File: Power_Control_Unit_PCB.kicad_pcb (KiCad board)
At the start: 2 copper layers, 98.3 x 93.2 mm, 25 parts, among them J1 Molex_Conn_01x04, J2 WR-BHD_Conn_02x08_Odd_Even, J3 WR-BHD_Conn_02x04_Odd_Even, J4 WR-BHD_Conn_02x03_Odd_Even, J5 WR-BHD_Conn_02x17_Odd_Even, U1 TSR_1-2433, U2 TSR_1-2450, U3 TSR3-24120N

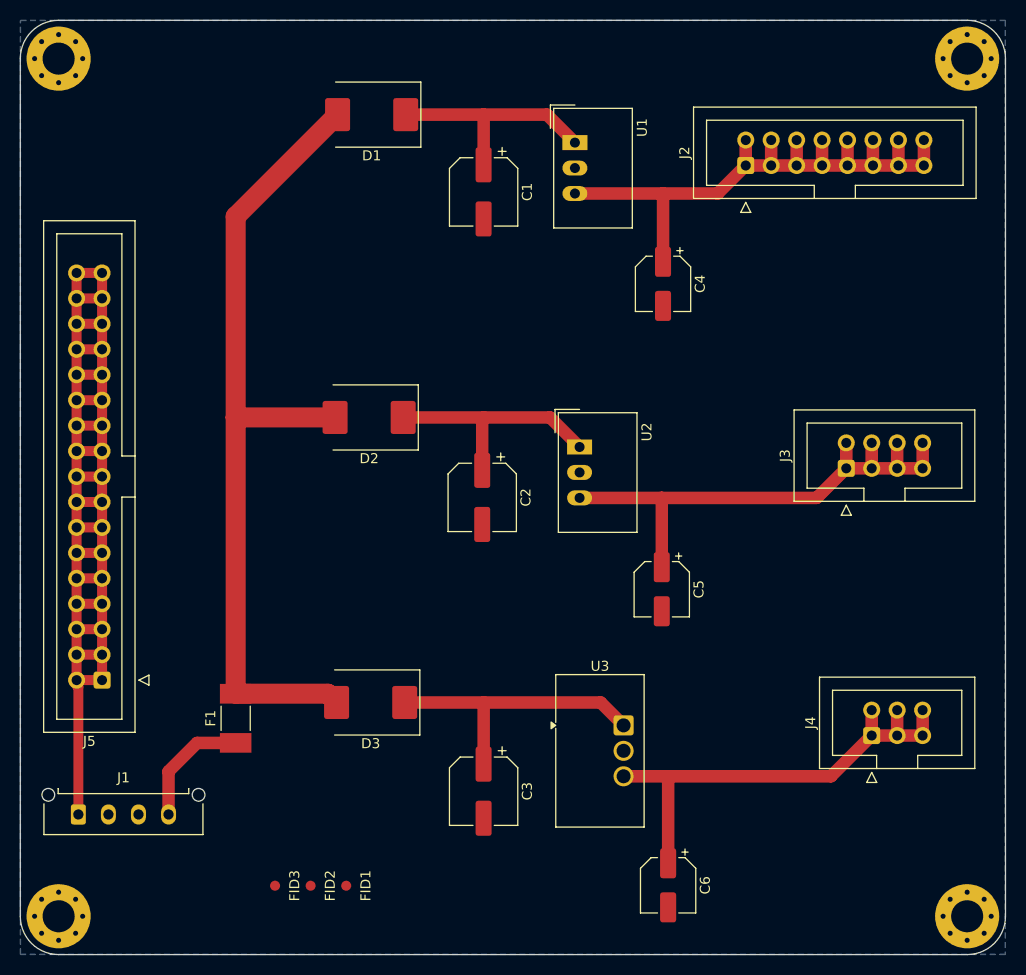
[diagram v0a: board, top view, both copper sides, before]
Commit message: PCU pcb design and added copper zones por power planes
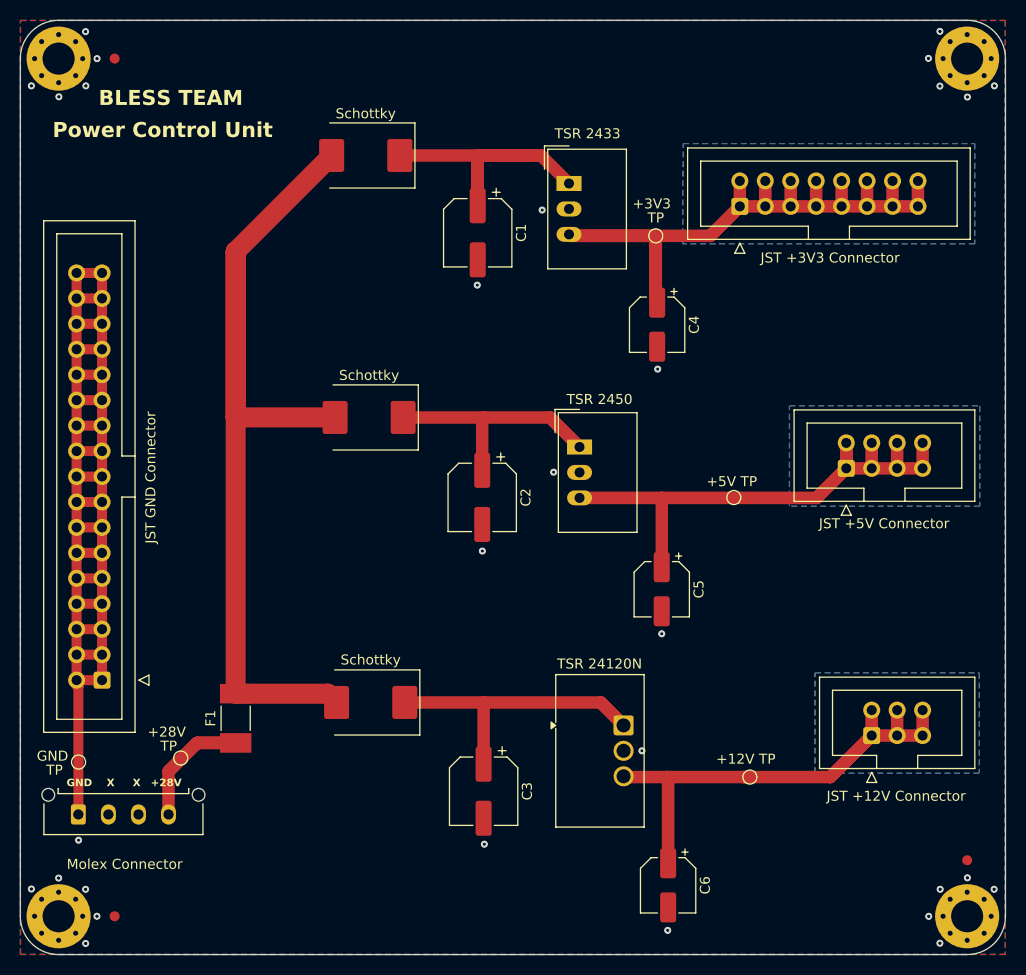
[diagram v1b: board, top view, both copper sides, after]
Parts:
- added TP1: TestPoint, TestPoint:TestPoint_Pad_D1.0mm, F.Cu at (124.7, 117.8)
- added TP2: TestPoint, TestPoint:TestPoint_Pad_D1.0mm, F.Cu at (172.1, 65.7)
- added TP3: TestPoint, TestPoint:TestPoint_Pad_D1.0mm, F.Cu at (179.9, 91.8)
- added TP4: TestPoint, TestPoint:TestPoint_Pad_D1.0mm, F.Cu at (181.5, 119.7)
- added TP5: TestPoint, TestPoint:TestPoint_Pad_D1.0mm, F.Cu at (114.5, 118.2)
- moved FID2 84.8 mm to (118.1, 48.0)
- moved FID1 62.0 mm to (203.2, 128.0)
- moved FID3 16.3 mm to (118.1, 133.6)
- moved C1 4.12 mm to (154.3, 65.4)
- moved U1 4.12 mm to (163.5, 60.5)
- moved C4 4.12 mm to (172.3, 74.6)
- moved D1 4.12 mm to (143.2, 57.7)
- moved J2 4.12 mm to (180.5, 62.8)
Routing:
- net +3V3: track 63.1 -> 92.5 mm
- net Net-(D1-A): track 82.4 -> 95.8 mm
- net Net-(D1-K): track 23.1 -> 34.4 mm
- net +12V: track 47.8 -> 57.2 mm
- net +28V: track 12.2 -> 20.1 mm
- net +5V: track 52.5 -> 59.2 mm
- net Net-(D2-K): track 24.2 -> 28.3 mm
- net Net-(D3-K): track 28.9 -> 32.2 mm
- net GND: track 137.9 -> 138.7 mm, vias 0 -> 30
- added copper zone on B.Cu, net +12V
- added copper zone on B.Cu, net +3V3
- added copper zone on B.Cu, net +5V
- added copper zone on F.Cu, net GND
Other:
- board text added: "+28V"
- board text added: "BLESS TEAM"
- board text added: "GND"
- board text added: "Power Control Unit"
- board text added: "X"
